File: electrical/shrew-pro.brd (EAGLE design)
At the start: 18 x 27 mm, 55 parts, among them IC1 LMR16006YQ3DDCTQ1, U1 ESP32-PICO-D4, U2 SX1280IMLTRT, U3 DRV8244SQRYJRQ1, U4 DRV8244SQRYJRQ1, X1 PIN-1X-BIG, X2 PIN-1X-BIG, X3 PIN-1X-BIG, X4 PIN-1X-BIG, X5 PIN-1X-BIG, X6 PIN-1X-BIG, Y1 52MHz TCXO

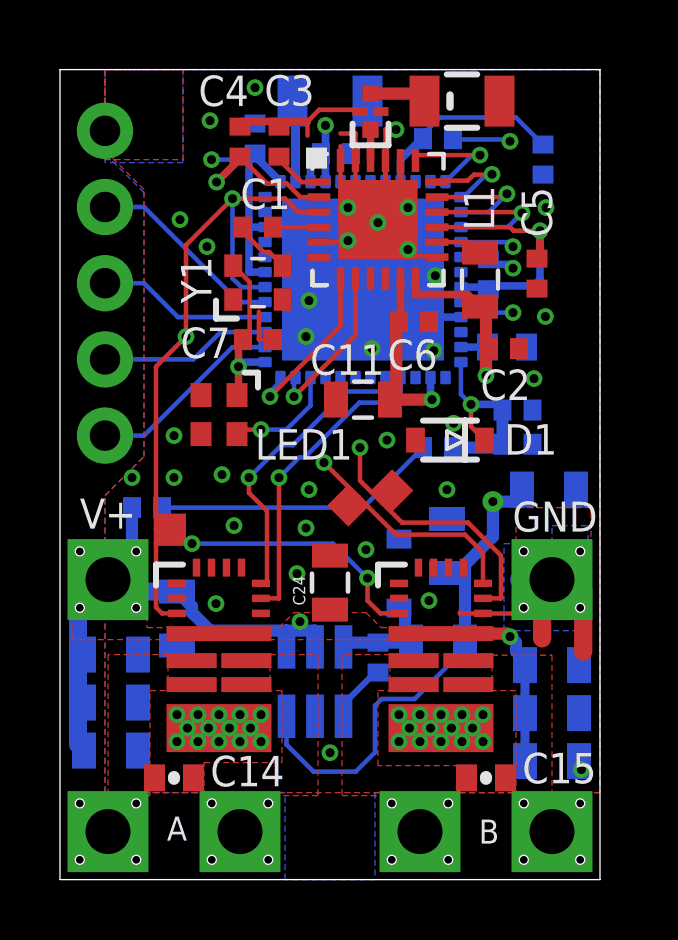
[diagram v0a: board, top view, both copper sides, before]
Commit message: sorted component ref des
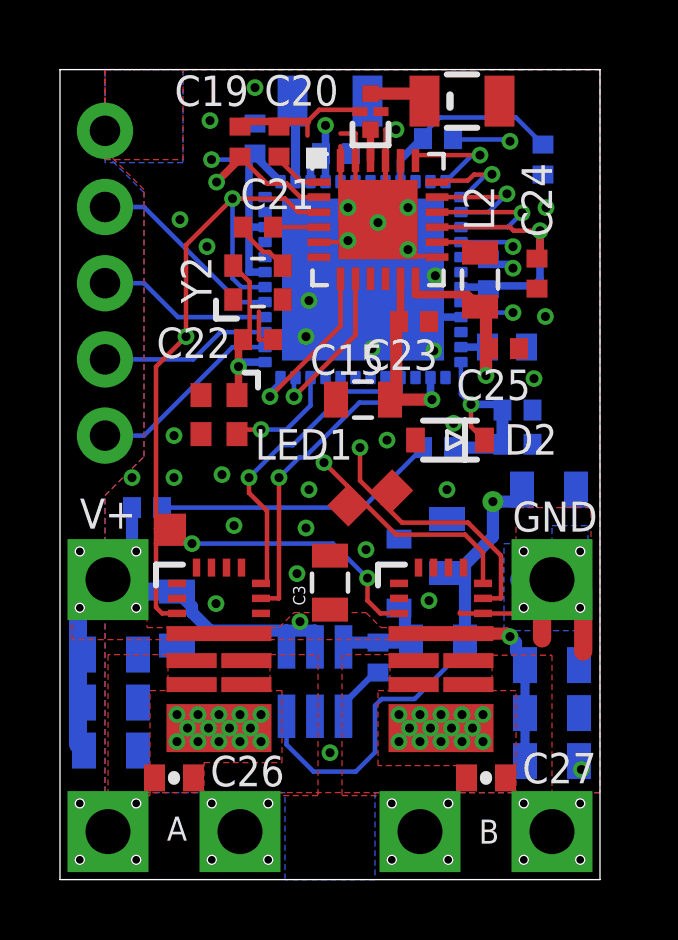
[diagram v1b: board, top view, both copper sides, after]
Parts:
- removed FL1: 2450FM07D0034T, shrew-core:FIL_2450FM07D0034T
- added Y2: 52MHz TCXO, shrew-common:OSC_TG2016SMN_50.0000M-ECGNNMB
- C1: value 1n -> 100n
- C10, C5, C6, C7, C8, C9: value 100n -> 10u; device shrew-common:0402-REV -> shrew-common:0805
- C11: value 10uF 25V -> 10u
- C12: value DNP -> 100n; device shrew-common:0402-CAP -> shrew-common:0402-REV
- C13: value 470n -> 100n
- C14: device shrew-common:0402-CAP -> shrew-common:0402-REV
- C15: value 100n -> 10uF 25V; device shrew-common:0402-CAP -> shrew-common:0805
- C16, C18, C25: value 10u -> 470n; device shrew-common:0805 -> shrew-common:0402-REV
- C17: value 470n -> DNP; device shrew-common:0402-REV -> shrew-common:0402-CAP
- C19, C20: value 10u -> 10n; device shrew-common:0805 -> shrew-common:0402-REV
- C2: value 470n -> 10u; device shrew-common:0402-REV -> shrew-common:0805
- C21: value 10u -> 1n; device shrew-common:0805 -> shrew-common:0402-REV
- C22, C23, C24: value 10u -> 100n; device shrew-common:0805 -> shrew-common:0402-REV
- C26: device shrew-common:0402-REV -> shrew-common:0402-CAP
- C27: value 10u -> 100n; device shrew-common:0805 -> shrew-common:0402-CAP
- C3, C4: value 10n -> 10u; device shrew-common:0402-REV -> shrew-common:0805
- D1: value 3V6 -> (none)
- D2: value (none) -> 3V6
- L1: value 15u -> 6u8
- L2: value 6u8 -> 15u
- R2: value 10K -> 68K
- R4: value 68K -> 10K
- U3, U4: value DRV8244SQRYJRQ1 -> DRV8244HQRYJRQ1
- Y1: value 52MHz TCXO -> 2450FM07D0034T; device shrew-common:OSC_TG2016SMN_50.0000M-ECGNNMB -> shrew-core:FIL_2450FM07D0034T
- moved C16 24.4 mm to (16.1, 24.0), turned to 90 degrees
- moved C10 21.6 mm to (16.4, 5.55), turned to 180 degrees
- moved C5 21.3 mm to (1.70, 4.30), flipped to the bottom, turned to 180 degrees
- moved C14 19.8 mm to (14.3, 20.2), flipped to the bottom, turned to 90 degrees
- moved C19 17.6 mm to (6.00, 24.6), flipped to the top, turned to 270 degrees
- moved C21 17.6 mm to (6.60, 21.8), flipped to the top, turned to 0 degrees
- moved X5 17.0 mm to (16.4, 1.60)
- moved C18 16.7 mm to (15.2, 15.7)
- moved C8 16.4 mm to (3.90, 8.70), turned to 270 degrees
- moved C20 16.3 mm to (7.30, 24.6), flipped to the top
- moved C6 16.2 mm to (1.70, 5.90), flipped to the bottom
- moved C22 15.8 mm to (6.60, 18.0), flipped to the top
- moved C4 15.5 mm to (16.3, 13.0), flipped to the bottom, turned to 180 degrees
- moved C23 15.4 mm to (11.8, 18.6), flipped to the top
- moved C1 14.9 mm to (10.6, 7.40), flipped to the bottom, turned to 270 degrees
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- renumbered EDGE1 to JP1
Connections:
- net +24V: now also C10.1, C11.1, C3.1, C5.1, C6.1, C7.1, C8.1, C9.1, R2.2, X1.1; no longer C16.1, C18.1, C19.1, C20.1, C21.1, C22.1, C23.1, C24.1, R4.2, X5.1
- net 3.3V: now also C12.1, C13.1, C14.1, C15.1, C2.1, C22.2, C23.2, C24.2, C4.1, L1.2, Y2.4; no longer C10.1, C11.1, C25.1, C27.1, C5.2, C6.2, C7.2, C8.1, C9.1, L2.2, Y1.4
- net BATT-ADC: now also C18.1, D2.1, R4.2; no longer C17.1, D1.1, R2.2
- net ESP-BOOT: now also C17.2; no longer C12.2
- net ESP-EN: now also C16.2; no longer C13.2
- net GND: now also C12.2, C13.2, C14.2, C15.2, C16.1, C17.1, C19.1, C2.2, C20.1, C22.1, C23.1, C24.1, C25.1, C3.2, C4.2, C5.2, C6.2, C7.2, R4.1, X2.1, Y1.4, Y2.2; no longer C12.1, C13.1, C16.2, C17.2, C19.2, C2.1, C20.2, C21.2, C22.2, C23.2, C24.2, C25.2, C27.2, C3.1, C4.1, C5.1, C6.1, C7.1, FL1.2, FL1.4, R2.1, X6.1
- net MOTOR1: now also C26.1, X3.1; no longer C14.1, X2.1
- net MOTOR2: now also C26.2, X4.1; no longer C14.2, X1.1
- net MOTOR3: now also C27.1, X5.1; no longer C15.1, X4.1
- net MOTOR4: now also C27.2, X6.1; no longer C15.2, X3.1
- net N$10: now also C1.1, D1.1, L1.1; no longer C26.1, D2.1, L2.1
- net N$11: now also C20.2; no longer C3.2
- net N$2: now also C21.1, Y2.3; no longer C1.1, Y1.3
- net N$3: now also C21.2; no longer C1.2
- net N$4: now also C1.2; no longer C26.2
- net N$6: now also Y1.1; no longer FL1.1
- net N$7: now also Y1.3; no longer FL1.3
- net N$9: now also L2.2; no longer L1.2
- net RADIO-VDD: now also C19.2, C25.2, L2.1; no longer C2.2, C4.2, L1.1
- net V-ADC: now also R2.1; no longer R4.1

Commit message: shrew pro prototype sent off to manufacturing
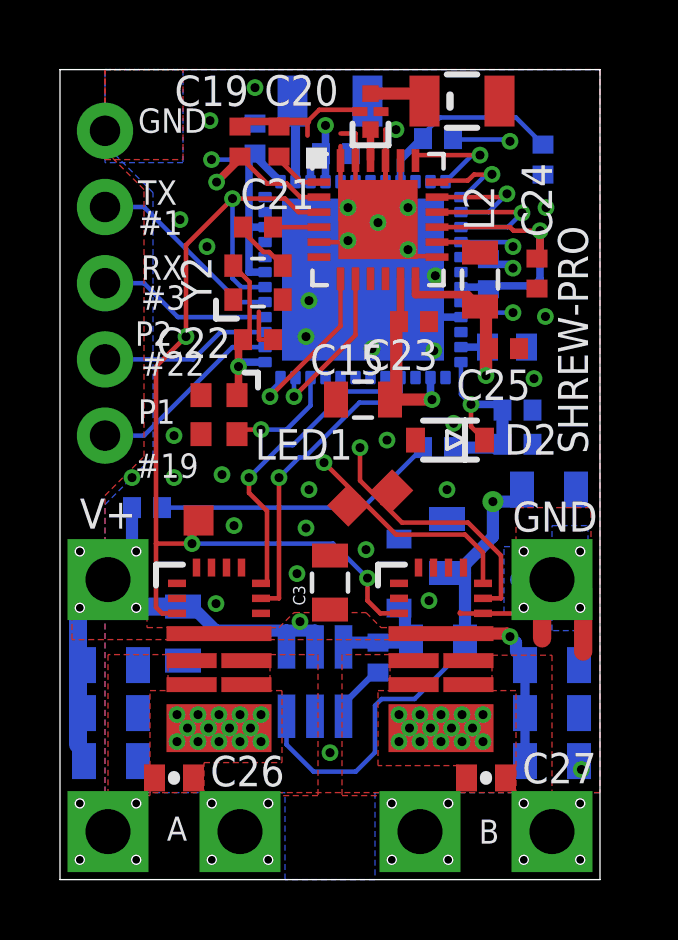
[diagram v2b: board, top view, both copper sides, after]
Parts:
- moved TP3 0.96 mm to (4.62, 12.0)
- moved C8 0.54 mm to (4.10, 8.20)
- moved C6 0.35 mm to (1.70, 5.55)
- moved C5 0.35 mm to (1.70, 3.95)
- moved C7 0.35 mm to (1.70, 7.15)
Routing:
- net GND: track 46.4 -> 50.3 mm
- net +24V: track 26.1 -> 27.0 mm
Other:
- board text added: "#1"
- board text added: "#19"
- board text added: "#22"
- board text added: "#3"
- board text removed: "1"
- board text removed: "19"
- board text removed: "22"
- board text removed: "3"
